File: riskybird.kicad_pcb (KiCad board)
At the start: 2 copper layers, 10 parts, among them U1 MCP73831-2-OT, U2 MPU-9150, U3 ESP32-WROOM-32, U3 TPS2113A, U4 ESP32-S3-WROOM-2

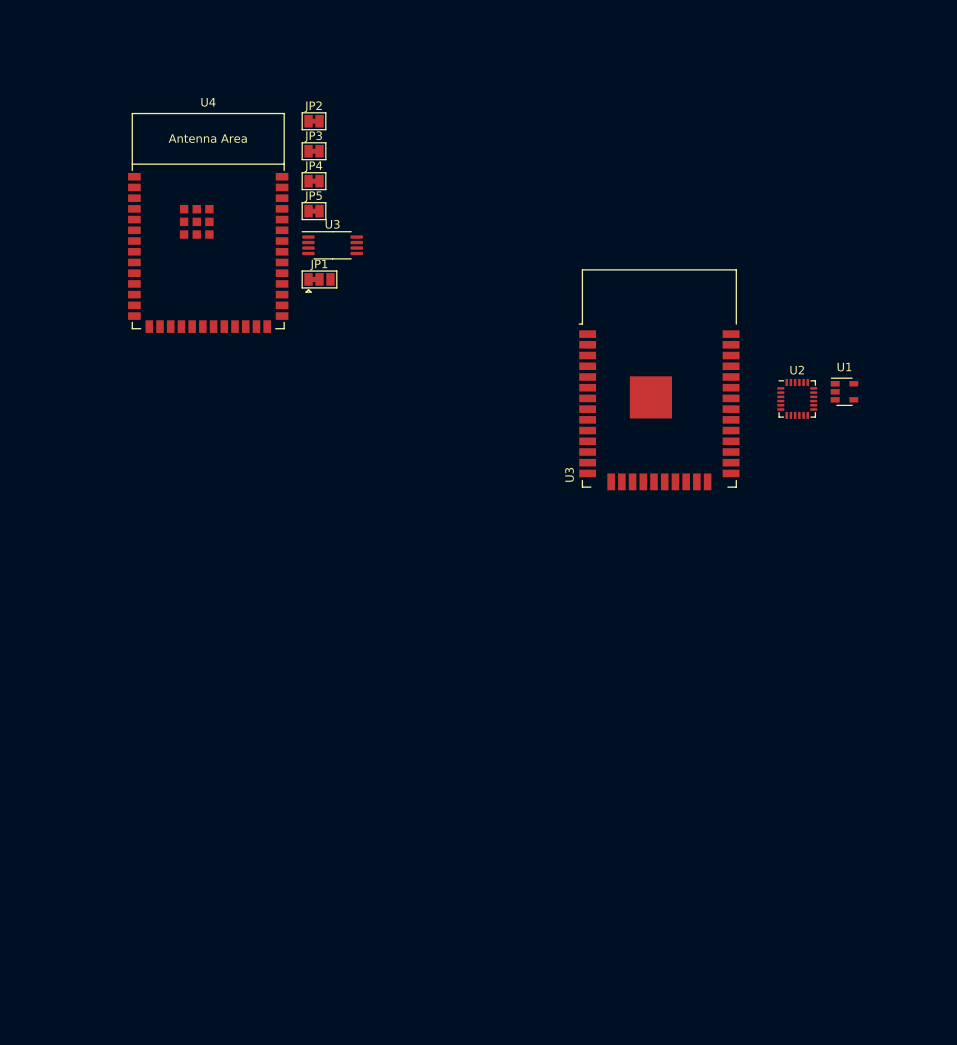
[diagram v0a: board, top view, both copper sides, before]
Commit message: update schematic with USB-UART, IMU, and Power
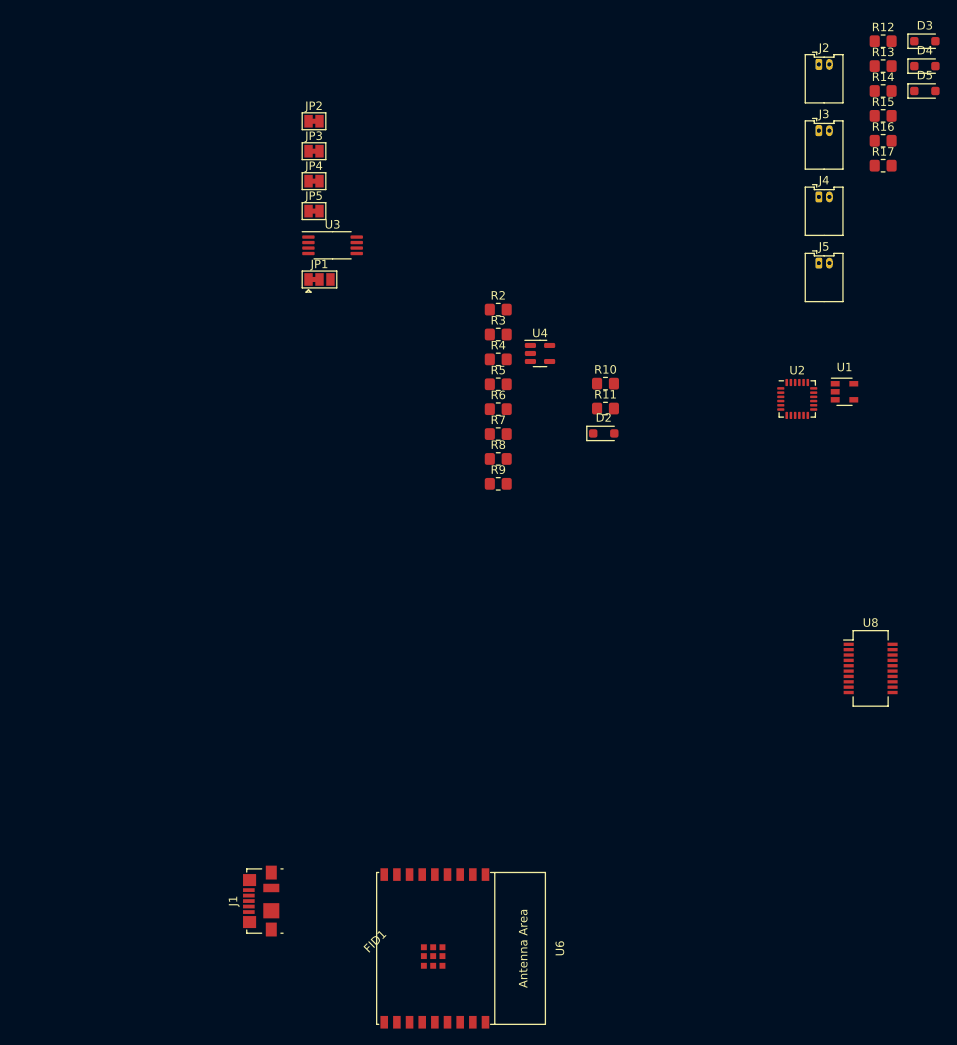
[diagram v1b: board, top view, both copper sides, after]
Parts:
- removed the U3 at (165.4, 12.1)
- added D2: BAT54JFILM, Diode_SMD:D_SOD-323_HandSoldering, F.Cu at (158.8, 15.7)
- added D3: BAT54JFILM, Diode_SMD:D_SOD-323_HandSoldering, F.Cu at (196.9, -30.8)
- added D4: BAT54JFILM, Diode_SMD:D_SOD-323_HandSoldering, F.Cu at (196.9, -27.9)
- added D5: BAT54JFILM, Diode_SMD:D_SOD-323_HandSoldering, F.Cu at (196.9, -24.9)
- added FID1: DroneFrame, riskybird:riskybird_frame, F.Cu at (132.1, 76.2)
- added J1: USB_B_Micro, Connector_USB:USB_Micro-B_Molex_47346-0001, F.Cu at (118.2, 71.1)
- added J2: Conn_01x02, Connector_Molex:Molex_PicoBlade_53048-0210_1x02_P1.25mm_Horizontal, F.Cu at (184.3, -28.1)
- added J3: Conn_01x02, Connector_Molex:Molex_PicoBlade_53048-0210_1x02_P1.25mm_Horizontal, F.Cu at (184.3, -20.2)
- added J4: Conn_01x02, Connector_Molex:Molex_PicoBlade_53048-0210_1x02_P1.25mm_Horizontal, F.Cu at (184.3, -12.4)
- added J5: Conn_01x02, Connector_Molex:Molex_PicoBlade_53048-0210_1x02_P1.25mm_Horizontal, F.Cu at (184.3, -4.53)
- added R10: 10k, Resistor_SMD:R_0805_2012Metric_Pad1.20x1.40mm_HandSolder, F.Cu at (159.0, 9.75)
- added R11: 47R, Resistor_SMD:R_0805_2012Metric_Pad1.20x1.40mm_HandSolder, F.Cu at (159.0, 12.7)
- added R12: 47R, Resistor_SMD:R_0805_2012Metric_Pad1.20x1.40mm_HandSolder, F.Cu at (191.9, -30.8)
- added R13: 10k, Resistor_SMD:R_0805_2012Metric_Pad1.20x1.40mm_HandSolder, F.Cu at (191.9, -27.9)
- added R14: 47R, Resistor_SMD:R_0805_2012Metric_Pad1.20x1.40mm_HandSolder, F.Cu at (191.9, -24.9)
- added R15: 10k, Resistor_SMD:R_0805_2012Metric_Pad1.20x1.40mm_HandSolder, F.Cu at (191.9, -22.0)
- added R16: 47R, Resistor_SMD:R_0805_2012Metric_Pad1.20x1.40mm_HandSolder, F.Cu at (191.9, -19.0)
- added R17: 10k, Resistor_SMD:R_0805_2012Metric_Pad1.20x1.40mm_HandSolder, F.Cu at (191.9, -16.1)
- added R2: 150, Resistor_SMD:R_0805_2012Metric_Pad1.20x1.40mm_HandSolder, F.Cu at (146.3, 0.97)
- added R3: 150, Resistor_SMD:R_0805_2012Metric_Pad1.20x1.40mm_HandSolder, F.Cu at (146.3, 3.92)
- added R4: 10k, Resistor_SMD:R_0805_2012Metric_Pad1.20x1.40mm_HandSolder, F.Cu at (146.3, 6.88)
- added R5: 10k, Resistor_SMD:R_0805_2012Metric_Pad1.20x1.40mm_HandSolder, F.Cu at (146.3, 9.82)
- added R6: 10k, Resistor_SMD:R_0805_2012Metric_Pad1.20x1.40mm_HandSolder, F.Cu at (146.3, 12.8)
- added R7: 10k, Resistor_SMD:R_0805_2012Metric_Pad1.20x1.40mm_HandSolder, F.Cu at (146.3, 15.7)
- added R8: 2.2k, Resistor_SMD:R_0805_2012Metric_Pad1.20x1.40mm_HandSolder, F.Cu at (146.3, 18.7)
- added R9: 2.2k, Resistor_SMD:R_0805_2012Metric_Pad1.20x1.40mm_HandSolder, F.Cu at (146.3, 21.6)
- added U6: ESP32-C3-WROOM-02, Espressif:ESP32-C3-WROOM-02, F.Cu at (138.9, 76.7)
- added U8: FT231XS, Package_SO:SSOP-20_3.9x8.7mm_P0.635mm, F.Cu at (190.4, 43.5)
- U4: value ESP32-S3-WROOM-2 -> LP2985-3.0; footprint Espressif:ESP32-S3-WROOM-2 -> Package_TO_SOT_SMD:SOT-23-5
- moved U4 41.3 mm to (151.3, 6.17)
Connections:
- JP1 pad 1: GNDA -> GND
- JP2 pad 2: GNDA -> GND
- JP3 pad 2: GNDA -> GND
- U1 pad 2: Net-(U1-VSS) -> GND
- U1 pad 4: /VUSB -> +5V
- U2 pad 15: GNDA -> GND
- U2 pad 17: GNDA -> GND
- U2 pad 18: GNDA -> GND
- U3 pad 1: unconnected-(U3-STAT-Pad1) -> Net-(U3-STAT)
- U3 pad 3: unconnected-(U3-VSNS-Pad3) -> Net-(U3-VSNS)
- U3 pad 6: /VBAT -> +BATT
- U3 pad 8: unconnected-(U3-IN1-Pad8) -> +5V
- U4 pad 1: Net-(U4-GND-Pad1) -> VCOM
- U4 pad 2: unconnected-(U4-3V3-Pad2) -> GND
- U4 pad 3: unconnected-(U4-EN-Pad3) -> /VEN_D
- U4 pad 4: unconnected-(U4-GPIO4/TOUCH4/ADC1_CH3-Pad4) -> Net-(U4-BP)
- U4 pad 5: unconnected-(U4-GPIO5/TOUCH5/ADC1_CH4-Pad5) -> VDD

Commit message: add baro footprint, switches, make passives 0603
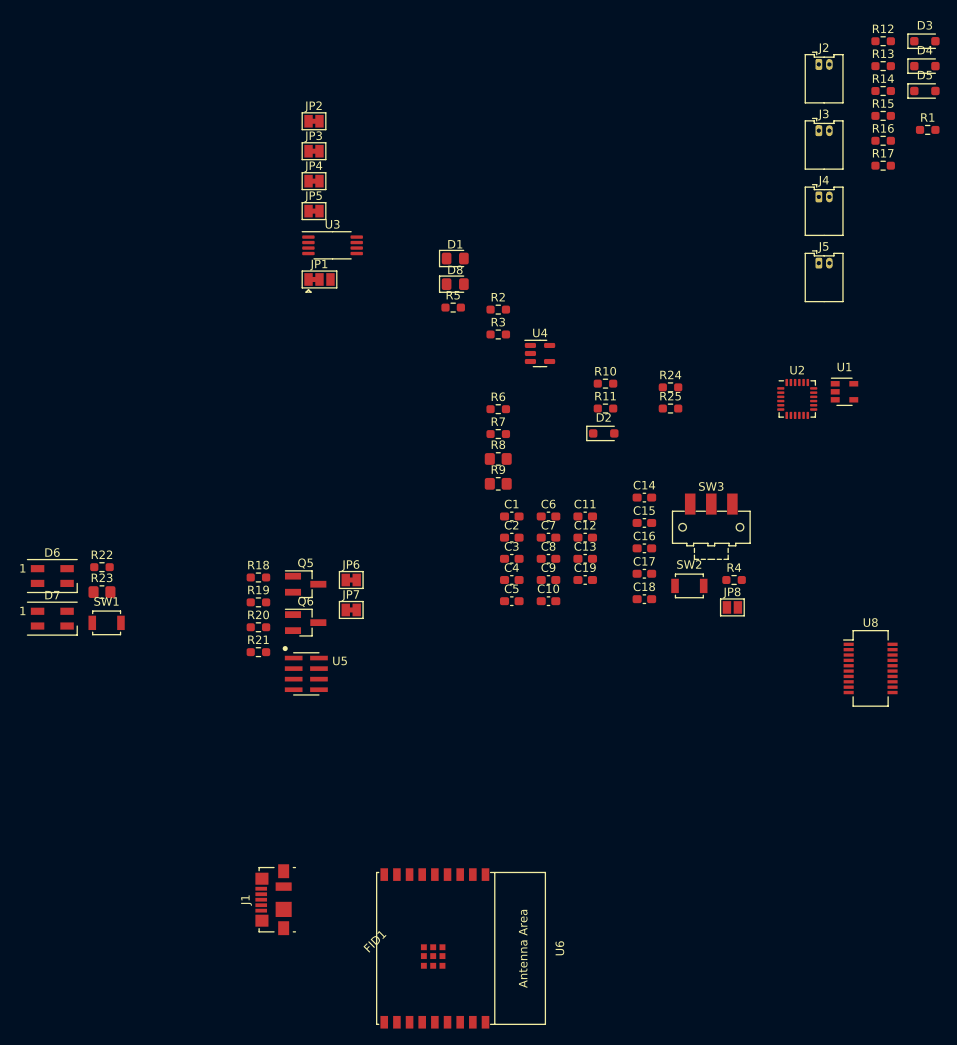
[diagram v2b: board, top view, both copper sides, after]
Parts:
- added C1: 4.7u, Capacitor_SMD:C_0603_1608Metric_Pad1.08x0.95mm_HandSolder, F.Cu at (147.9, 25.5)
- added C10: 4.7u, Capacitor_SMD:C_0603_1608Metric_Pad1.08x0.95mm_HandSolder, F.Cu at (152.3, 35.5)
- added C11: 10n, Capacitor_SMD:C_0603_1608Metric_Pad1.08x0.95mm_HandSolder, F.Cu at (156.6, 25.5)
- added C12: 4.7u, Capacitor_SMD:C_0603_1608Metric_Pad1.08x0.95mm_HandSolder, F.Cu at (156.6, 28.0)
- added C13: 0.1u, Capacitor_SMD:C_0603_1608Metric_Pad1.08x0.95mm_HandSolder, F.Cu at (156.6, 30.5)
- added C14: 0.1u, Capacitor_SMD:C_0603_1608Metric_Pad1.08x0.95mm_HandSolder, F.Cu at (163.6, 23.2)
- added C15: 0.1u, Capacitor_SMD:C_0603_1608Metric_Pad1.08x0.95mm_HandSolder, F.Cu at (163.6, 26.3)
- added C16: 10u, Capacitor_SMD:C_0603_1608Metric_Pad1.08x0.95mm_HandSolder, F.Cu at (163.6, 29.3)
- added C17: 0.1u, Capacitor_SMD:C_0603_1608Metric_Pad1.08x0.95mm_HandSolder, F.Cu at (163.6, 32.3)
- added C18: 0.1u, Capacitor_SMD:C_0603_1608Metric_Pad1.08x0.95mm_HandSolder, F.Cu at (163.6, 35.3)
- added C19: 1u, Capacitor_SMD:C_0603_1608Metric_Pad1.08x0.95mm_HandSolder, F.Cu at (156.6, 33.0)
- added C2: 4.7u, Capacitor_SMD:C_0603_1608Metric_Pad1.08x0.95mm_HandSolder, F.Cu at (147.9, 28.0)
- added C3: 0.1u, Capacitor_SMD:C_0603_1608Metric_Pad1.08x0.95mm_HandSolder, F.Cu at (147.9, 30.5)
- added C4: 10n, Capacitor_SMD:C_0603_1608Metric_Pad1.08x0.95mm_HandSolder, F.Cu at (147.9, 33.0)
- added C5: 0.1u, Capacitor_SMD:C_0603_1608Metric_Pad1.08x0.95mm_HandSolder, F.Cu at (147.9, 35.5)
- added C6: 2.2n, Capacitor_SMD:C_0603_1608Metric_Pad1.08x0.95mm_HandSolder, F.Cu at (152.3, 25.5)
- added C7: 10u, Capacitor_SMD:C_0603_1608Metric_Pad1.08x0.95mm_HandSolder, F.Cu at (152.3, 28.0)
- added C8: 100n, Capacitor_SMD:C_0603_1608Metric_Pad1.08x0.95mm_HandSolder, F.Cu at (152.3, 30.5)
- added C9: 0.1u, Capacitor_SMD:C_0603_1608Metric_Pad1.08x0.95mm_HandSolder, F.Cu at (152.3, 33.0)
- added D1: LED_RED, LED_SMD:LED_0805_2012Metric_Pad1.15x1.40mm_HandSolder, F.Cu at (141.2, -5.08)
- added D6: SK6812MINI, LED_SMD:LED_SK6812MINI_PLCC4_3.5x3.5mm_P1.75mm, F.Cu at (93.5, 32.5)
- added D7: SK6812MINI, LED_SMD:LED_SK6812MINI_PLCC4_3.5x3.5mm_P1.75mm, F.Cu at (93.5, 37.6)
- added D8: LED_BLUE, LED_SMD:LED_0805_2012Metric_Pad1.15x1.40mm_HandSolder, F.Cu at (141.2, -2.04)
- added JP6: SolderJumper_2_Bridged, Jumper:SolderJumper-2_P1.3mm_Bridged_Pad1.0x1.5mm, F.Cu at (128.9, 33.0)
- added JP7: SolderJumper_2_Bridged, Jumper:SolderJumper-2_P1.3mm_Bridged_Pad1.0x1.5mm, F.Cu at (128.9, 36.6)
- added JP8: SolderJumper_2_Open, Jumper:SolderJumper-2_P1.3mm_Open_Pad1.0x1.5mm, F.Cu at (174.1, 36.3)
- added Q5: DNBT8105-7, Package_TO_SOT_SMD:SOT-23_Handsoldering, F.Cu at (123.5, 33.5)
- added Q6: DNBT8105-7, Package_TO_SOT_SMD:SOT-23_Handsoldering, F.Cu at (123.5, 38.1)
- added R1: 2k, Resistor_SMD:R_0603_1608Metric_Pad0.98x0.95mm_HandSolder, F.Cu at (197.2, -20.3)
- added R18: 27, Resistor_SMD:R_0603_1608Metric_Pad0.98x0.95mm_HandSolder, F.Cu at (117.9, 32.7)
- added R19: 27, Resistor_SMD:R_0603_1608Metric_Pad0.98x0.95mm_HandSolder, F.Cu at (117.9, 35.7)
- added R20: 10k, Resistor_SMD:R_0603_1608Metric_Pad0.98x0.95mm_HandSolder, F.Cu at (117.9, 38.6)
- added R21: 10k, Resistor_SMD:R_0603_1608Metric_Pad0.98x0.95mm_HandSolder, F.Cu at (117.9, 41.6)
- added R22: 10k, Resistor_SMD:R_0603_1608Metric_Pad0.98x0.95mm_HandSolder, F.Cu at (99.3, 31.5)
- added R23: 10k, Resistor_SMD:R_0805_2012Metric_Pad1.20x1.40mm_HandSolder, F.Cu at (99.3, 34.5)
- added R24: 20k, Resistor_SMD:R_0603_1608Metric_Pad0.98x0.95mm_HandSolder, F.Cu at (166.7, 10.2)
- added R25: 10k, Resistor_SMD:R_0603_1608Metric_Pad0.98x0.95mm_HandSolder, F.Cu at (166.7, 12.7)
- added SW1: SW_SPST, Button_Switch_SMD:SW_SPST_B3U-1000P, F.Cu at (99.9, 38.1)
- added SW2: SW_SPST, Button_Switch_SMD:SW_SPST_B3U-1000P, F.Cu at (169.0, 33.7)
- added SW3: SW_SPST, Button_Switch_SMD:SW_SPDT_CK-JS102011SAQN, F.Cu at (171.6, 26.8)
- added U5: MPL3115A2, riskybird:MPL3115A2, F.Cu at (123.6, 44.1)
- R10, R11, R12, R13, R14, R15, R16, R17, R2, R3, R6, R7: footprint Resistor_SMD:R_0805_2012Metric_Pad1.20x1.40mm_HandSolder -> Resistor_SMD:R_0603_1608Metric_Pad0.98x0.95mm_HandSolder
- R4: value 10k -> 100k; footprint Resistor_SMD:R_0805_2012Metric_Pad1.20x1.40mm_HandSolder -> Resistor_SMD:R_0603_1608Metric_Pad0.98x0.95mm_HandSolder
- R5: value 10k -> 150; footprint Resistor_SMD:R_0805_2012Metric_Pad1.20x1.40mm_HandSolder -> Resistor_SMD:R_0603_1608Metric_Pad0.98x0.95mm_HandSolder
- moved R4 38.3 mm to (174.3, 33.0)
- moved R5 10.5 mm to (141.0, 0.73)
- moved J1 1.47 mm to (119.7, 70.9)
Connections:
- J1 pad 2: unconnected-(J1-D--Pad2) -> /USB_DM
- J1 pad 3: unconnected-(J1-D+-Pad3) -> /USB_DP
- R4 pad 1: +5V -> /VEN_D
- R4 pad 2: /VEN_D -> GND
- R5 pad 1: /VEN_D -> VDD
- R5 pad 2: GND -> Net-(D8-A)
- U6 pad 11: unconnected-(U6-GPIO20/U0RXD-Pad11) -> /U0RXD
- U6 pad 12: unconnected-(U6-GPIO21/U0TXD-Pad12) -> /U0TXD
- U6 pad 13: unconnected-(U6-GPIO18/USB_D--Pad13) -> /INT_IMU
- U6 pad 14: unconnected-(U6-GPIO19/USB_D+-Pad14) -> /INT1_BARO
- U6 pad 15: unconnected-(U6-GPIO3/ADC1_CH3-Pad15) -> /MOTOR2
- U6 pad 16: unconnected-(U6-GPIO2/ADC1_CH2-Pad16) -> /MOTOR1
- U6 pad 18: unconnected-(U6-GPIO0/ADC1_CH0/XTAL_32K_P-Pad18) -> /VSENSE
- U6 pad 2: unconnected-(U6-EN/CHIP_PU-Pad2) -> /CHIP_EN
- U6 pad 3: unconnected-(U6-GPIO4/ADC1_CH4-Pad3) -> /MOTOR3
- U6 pad 4: unconnected-(U6-GPIO5/ADC2_CH0-Pad4) -> /MOTOR4
- U6 pad 7: unconnected-(U6-GPIO8-Pad7) -> /RGB_CTRL
- U6 pad 8: unconnected-(U6-GPIO9-Pad8) -> /GPIO9
- U8 pad 1: unconnected-(U8-~{DTR}-Pad1) -> /DTR
- U8 pad 11: unconnected-(U8-USBDP-Pad11) -> Net-(U8-USBDP)
- U8 pad 12: unconnected-(U8-USBDM-Pad12) -> Net-(U8-USBDM)
- U8 pad 14: unconnected-(U8-~{RESET}-Pad14) -> VDD
- U8 pad 15: unconnected-(U8-VCC-Pad15) -> +5V
- U8 pad 16: unconnected-(U8-GND-Pad16) -> GND
- U8 pad 2: unconnected-(U8-~{RTS}-Pad2) -> /RTS
- U8 pad 20: unconnected-(U8-TXD-Pad20) -> Net-(JP6-A)
- U8 pad 3: unconnected-(U8-VCCIO-Pad3) -> VDD
- U8 pad 4: unconnected-(U8-RXD-Pad4) -> Net-(JP7-A)
- U8 pad 6: unconnected-(U8-GND-Pad6) -> GND
